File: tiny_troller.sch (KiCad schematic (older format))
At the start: 32 parts, among them U1 MA702GQ-P, U3 STM32G071G8U6, U5 MCP2025-330E_MD, U6 MAX14870ETC+T

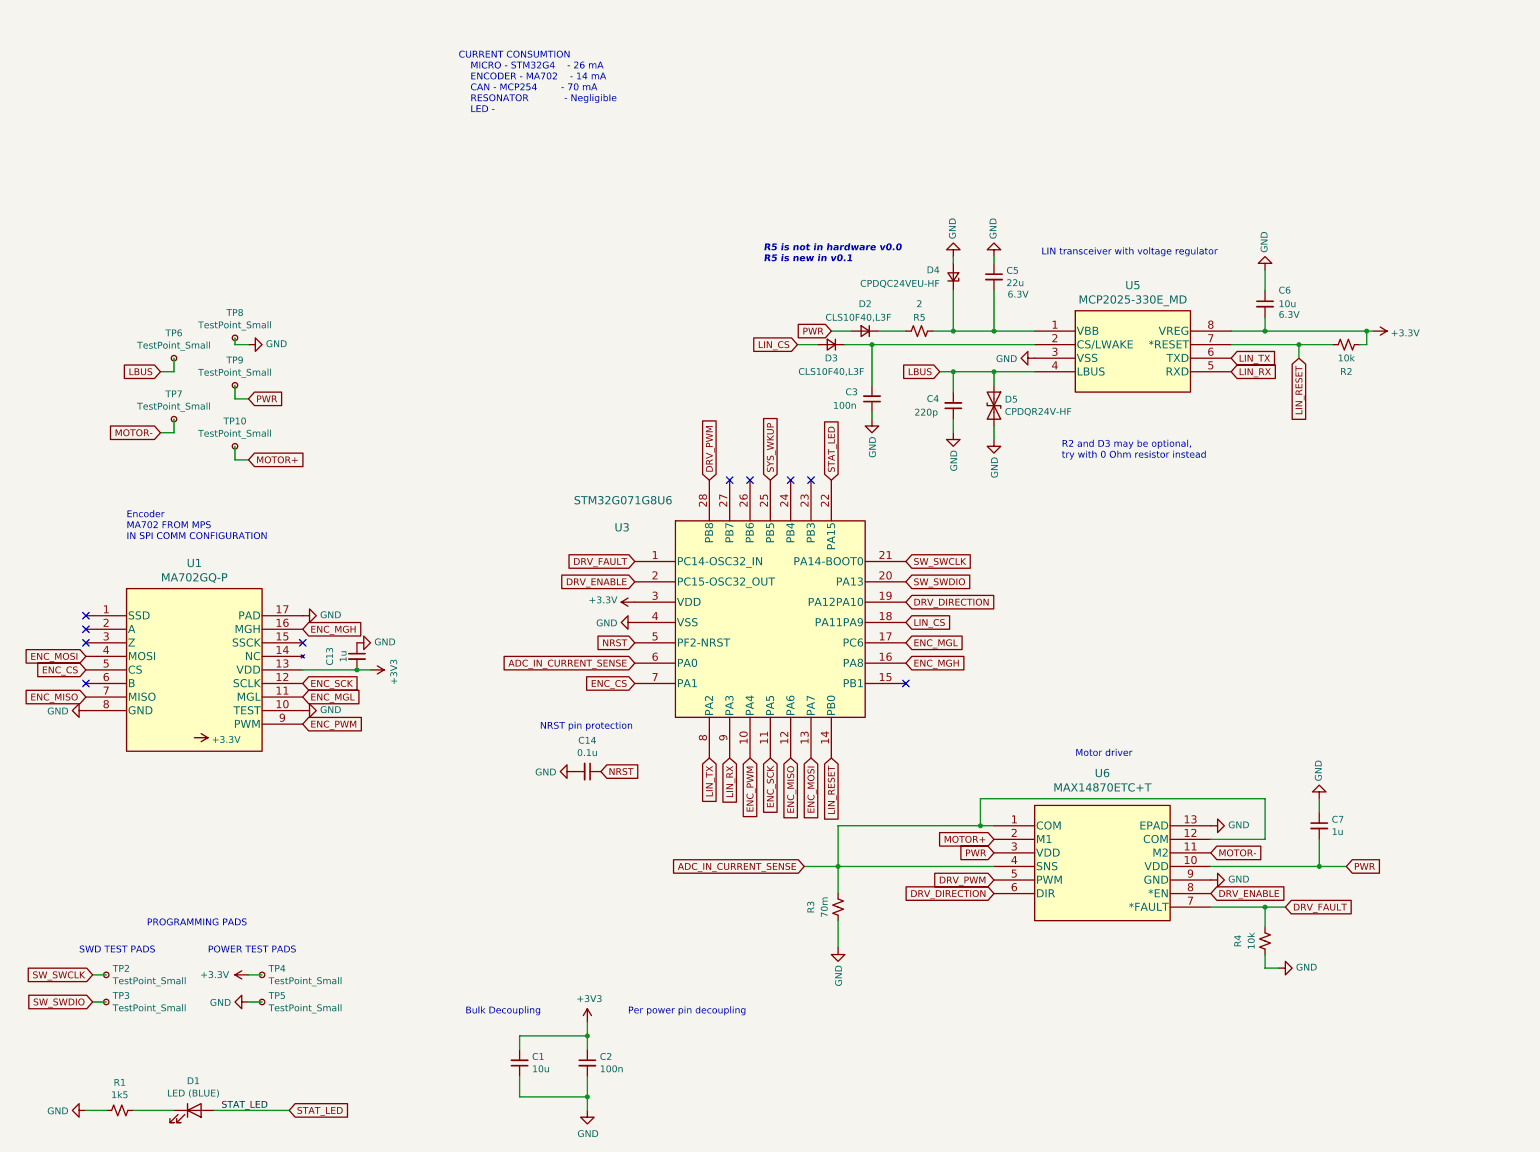
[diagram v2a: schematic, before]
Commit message: updated BOM for v00 and v01, needs one final look over with attention paid to maximum power and voltage ratings of passives
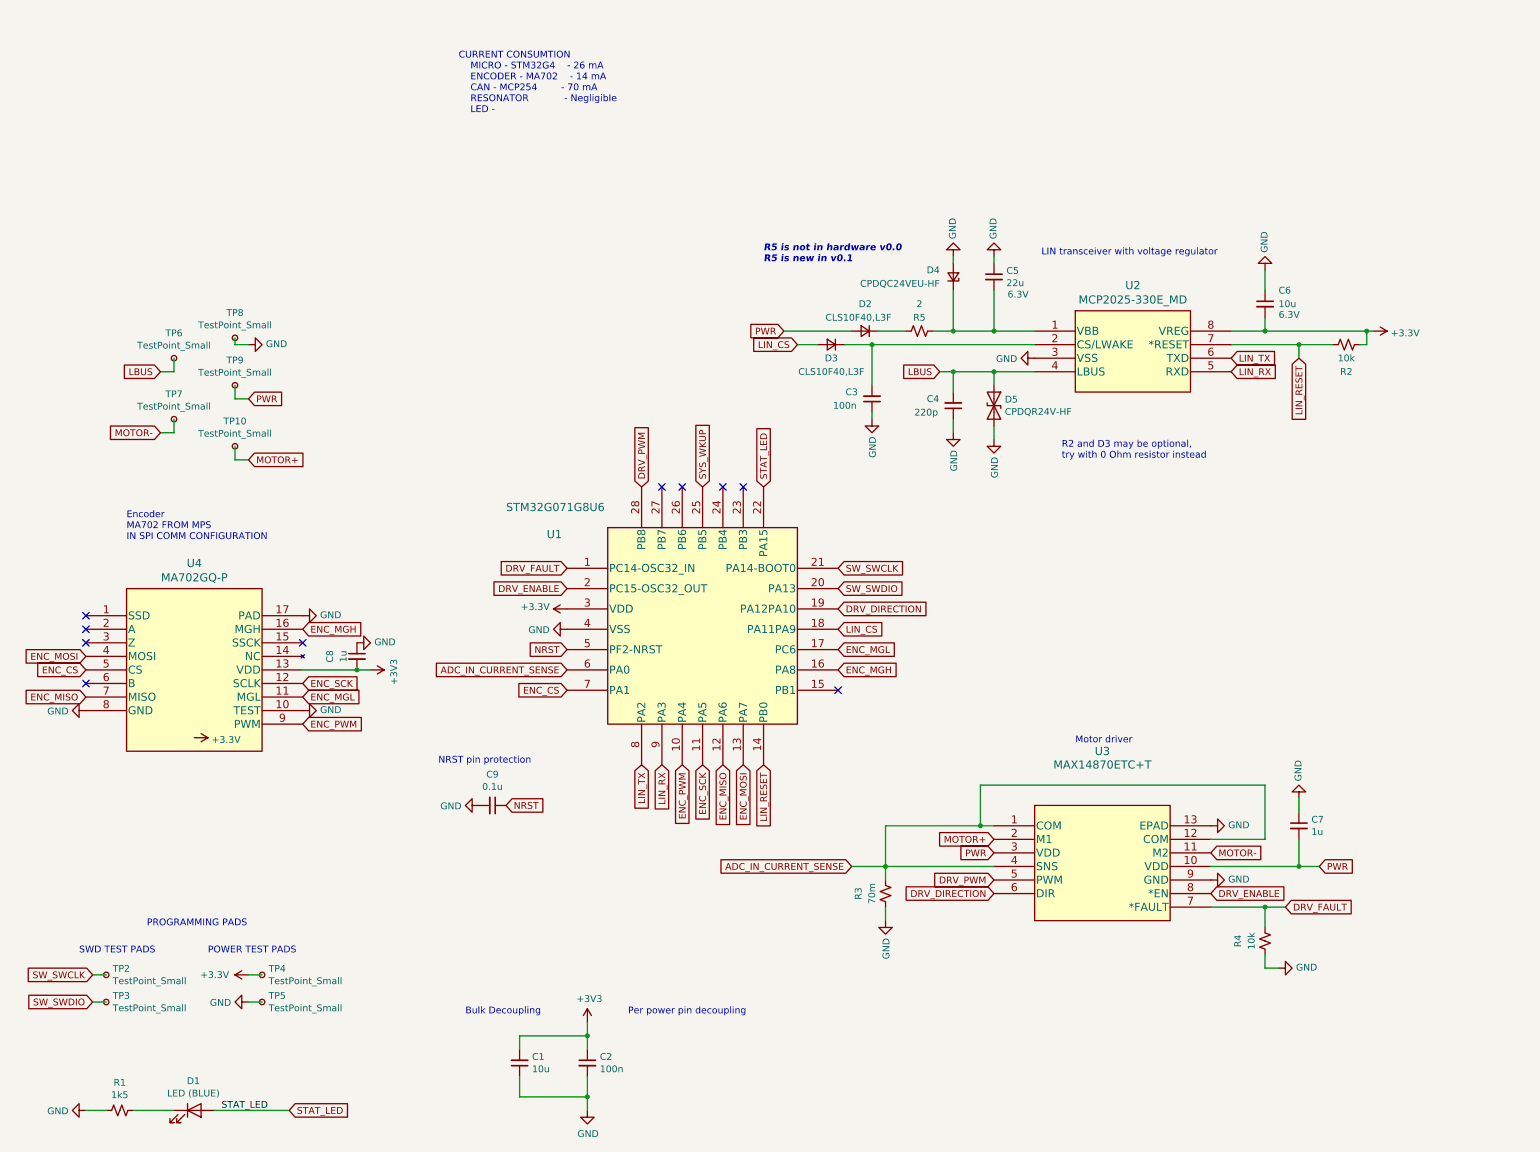
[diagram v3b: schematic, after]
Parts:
- renumbered C13 to C8, C14 to C9, U3 to U1, U5 to U2, U6 to U3, U1 to U4
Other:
- moved on the sheet: C7, C9, R3, U1
